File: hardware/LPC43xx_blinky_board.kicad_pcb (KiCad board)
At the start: 4 copper layers, 68 x 49.4 mm, 60 parts, among them J1 Conn_01x04_Male, J2 Conn_ARM_JTAG_SWD_10, J3 USB_B_Micro, J4 Conn_01x20_Female, J5 Micro_SD_Card, J6 Conn_01x04_Female, J7 Conn_01x08_Female, SW1 SW_DIP_x01, SW2 SW_DIP_x04, SW3 SW_SPST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

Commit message: Add final header and silkscreen
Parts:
- added G***: LOGO, Logo:blinky101_logo, B.Cu at (176.8, 93.2)
- added G***: LOGO, Logo:Jitter-med, B.Cu at (169.4, 85.1)
- added J8: Conn_01x16_Female, Connector_PinSocket_2.54mm:PinSocket_1x16_P2.54mm_Vertical, F.Cu at (184.0, 71.9)
- added MH1: MountingHole_Pad, MountingHole:MountingHole_3.2mm_M3_Pad_Via, F.Cu at (115.1, 108.1)
- added MH2: MountingHole_Pad, MountingHole:MountingHole_3.2mm_M3_Pad_Via, F.Cu at (183.6, 66.4)
- J7: footprint Connector_PinSocket_2.54mm:PinSocket_1x08_P2.54mm_Vertical -> Connector_PinSocket_2.54mm:PinSocket_1x09_P2.54mm_Vertical
- moved D1 3.34 mm to (176.5, 68.5)
- moved D2 3.34 mm to (171.8, 68.5)
- moved D3 3.34 mm to (167.8, 68.5)
- moved D4 3.34 mm to (162.0, 68.5)
- moved RN3 3.34 mm to (168.0, 73.8)
- moved J7 1.10 mm to (161.0, 109.6)
- moved SW1 0.25 mm to (120.8, 105.6)
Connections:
- J7 pad 5: Net-(J7-Pad5) -> /AD0
- J7 pad 6: Net-(J7-Pad6) -> /AD1
- J7 pad 7: /AD0 -> /SSP1_SCK
- J7 pad 8: /AD1 -> /SSP1_MISO
- U1 pad 32: Net-(U1-Pad32) -> /SSP1_MISO
- U1 pad 34: Net-(U1-Pad34) -> /SSP1_MOSI
- U1 pad 68: Net-(U1-Pad68) -> /SSP1_SCK
- U1 pad 73: Net-(U1-Pad73) -> /P6_0
- U1 pad 74: Net-(U1-Pad74) -> /P6_1
- U1 pad 78: Net-(U1-Pad78) -> /P6_2
- U1 pad 79: Net-(U1-Pad79) -> /P6_3
- U1 pad 80: Net-(U1-Pad80) -> /P6_4
- U1 pad 82: Net-(U1-Pad82) -> /P6_5
- U1 pad 83: Net-(U1-Pad83) -> /P6_6
- U1 pad 84: Net-(U1-Pad84) -> /P2_2
- U1 pad 85: Net-(U1-Pad85) -> /P6_7
- U1 pad 86: Net-(U1-Pad86) -> /P6_8
- U1 pad 87: Net-(U1-Pad87) -> /P2_3
- U1 pad 88: Net-(U1-Pad88) -> /P2_4
- U1 pad 91: Net-(U1-Pad91) -> /P2_5
- U1 pad 95: Net-(U1-Pad95) -> /P2_6
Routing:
- net /P2_6: track 0.00 -> 41.1 mm, vias 0 -> 1
- net /P2_5: track 0.00 -> 29.2 mm
- net /P2_4: track 0.00 -> 28.7 mm
- net /P6_0: track 0.00 -> 28.5 mm, vias 0 -> 1
- net /P2_3: track 0.00 -> 27.9 mm
- net /P6_1: track 0.00 -> 27.5 mm, vias 0 -> 1
- net /P6_2: track 0.00 -> 27.4 mm
- net /P6_8: track 0.00 -> 27.1 mm
- net /P6_3: track 0.00 -> 26.4 mm
- net /P6_7: track 0.00 -> 26.2 mm
- net /P6_4: track 0.00 -> 25.6 mm
- net /P2_2: track 0.00 -> 25.4 mm
- net /P6_5: track 0.00 -> 24.9 mm
- net /P6_6: track 0.00 -> 24.5 mm
- net /SSP1_SCK: track 0.00 -> 18.7 mm, vias 0 -> 2
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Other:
- board size 68 x 49.4 mm -> 76.2 x 49.5 mm
- board text added: "I2C0"
- board text added: "MISO"
- board text added: "MOSI"
- board text added: "Made in Delft"
- board text added: "P0_0"
- board text added: "P0_1"
- board text added: "P1_19"
- board text added: "P2_0"
- board text added: "P2_1"
- board text added: "P2_2"
- board text added: "P2_3"
- board text added: "P2_4"
- board text added: "P2_5"
- board text added: "P2_6"
- board text added: "P3_1"
- board text added: "P3_2"
- board text added: "P4_7"
- board text added: "P6_0"
- board text added: "P6_1"
- board text added: "P6_2"
- board text added: "P6_3"
- board text added: "P6_4"
- board text added: "P6_5"
- board text added: "P6_6"
- board text added: "P6_7"
- board text added: "P6_8"
- board text added: "P7_4"
- board text added: "P7_5"
- board text added: "P7_6"
- board text added: "P7_7"
- board text added: "PF_4"
- board text added: "RTC_ALARM"
- board text added: "SCK"
- board text added: "SSP1"
- board text added: "SWCLK"
- board text added: "SWDIO"
- board text added: "USART0"
- board text added: "V1.0 lpc43xx"
- board text added: "WakeUP0"
- board text added: "blinky101.github.io"

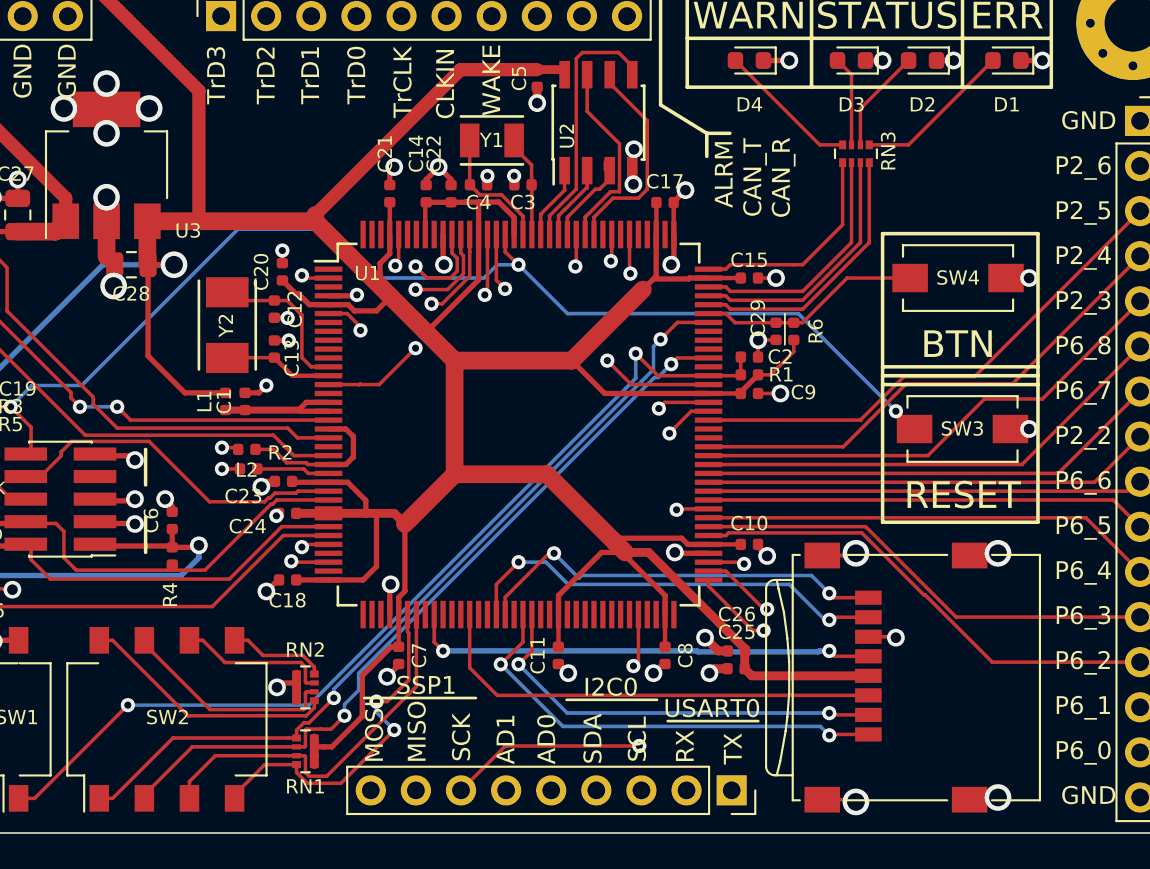
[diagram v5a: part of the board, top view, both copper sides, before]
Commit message: Add missing step files and fix some milimeter work
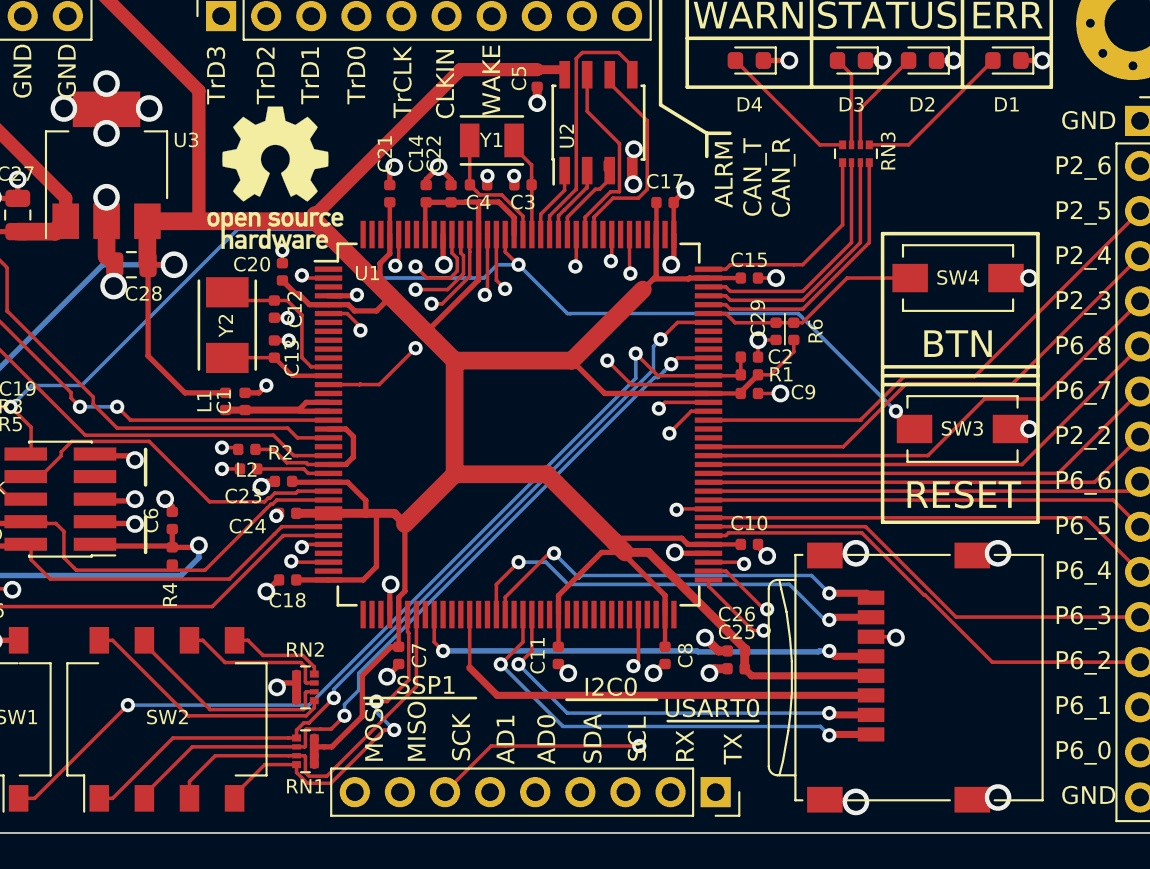
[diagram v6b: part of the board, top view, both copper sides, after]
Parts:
- added REF**: OSHW-Logo_7.5x8mm_SilkScreen, Symbol:OSHW-Logo_7.5x8mm_SilkScreen, F.Cu at (135.3, 75.1)
- moved J7 0.91 mm to (160.1, 109.7)
- moved J5 0.15 mm to (170.4, 103.2)
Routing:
- net /SSP1_SCK: track 18.7 -> 19.7 mm
- net /AD1: track 37.6 -> 36.7 mm
- net /SSP1_MISO: track 18.4 -> 17.6 mm

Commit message: Some silkscreen fixes
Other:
- board text added: "JTAG"
- board text added: "SWD"
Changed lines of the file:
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@@
   (general
     (thickness 1.6)
-    (drawings 118)
+    (drawings 126)
     (tracks 941)
     (zones 0)
@@
     (tags capacitor)
     (attr smd)
-    (fp_text reference C1 (at 0 -1.17 90) (layer F.SilkS)
+    (fp_text reference C1 (at -0.1 1.2 90) (layer F.SilkS)
       (effects (font (size 0.8 0.8) (thickness 0.1)))
     )
@@
     (tags capacitor)
     (attr smd)
-    (fp_text reference C8 (at 0 -1.17 270) (layer F.SilkS)
+    (fp_text reference C8 (at 0 0.85 270) (layer F.SilkS)
       (effects (font (size 0.8 0.8) (thickness 0.1)))
     )
@@
     (tags capacitor)
     (attr smd)
-    (fp_text reference C14 (at 2.25 -0.55 90) (layer F.SilkS)
+    (fp_text reference C14 (at 2.25 -0.8 90) (layer F.SilkS)
       (effects (font (size 0.8 0.8) (thickness 0.1)))
     )
@@
     (tags capacitor)
     (attr smd)
-    (fp_text reference C21 (at 2.25 -0.25 90) (layer F.SilkS)
+    (fp_text reference C21 (at 0 -1 90) (layer F.SilkS)
       (effects (font (size 0.8 0.8) (thickness 0.1)))
     )
@@
     (tags capacitor)
     (attr smd)
-    (fp_text reference C25 (at -0.05 2.05 180) (layer F.SilkS)
+    (fp_text reference C25 (at 2.25 0.15 180) (layer F.SilkS)
       (effects (font (size 0.8 0.8) (thickness 0.1)))
     )
@@
     (tags capacitor)
     (attr smd)
-    (fp_text reference C26 (at -0.035 2.05 180) (layer F.SilkS)
+    (fp_text reference C26 (at 0.065 1.15 180) (layer F.SilkS)
       (effects (font (size 0.8 0.8) (thickness 0.1)))
     )
@@
     (tags resistor)
     (attr smd)
-    (fp_text reference L1 (at 0 -1.17 90) (layer F.SilkS)
+    (fp_text reference L1 (at -0.1 -1.1 90) (layer F.SilkS)
       (effects (font (size 0.8 0.8) (thickness 0.1)))
     )
@@
     (tags resistor)
     (attr smd)
-    (fp_text reference L2 (at 0 -1.17 180) (layer F.SilkS)
+    (fp_text reference L2 (at 2.5 0.2 180) (layer F.SilkS)
       (effects (font (size 0.8 0.8) (thickness 0.1)))
     )
@@
     (tags resistor)
     (attr smd)
-    (fp_text reference R2 (at -1.8 0.9 180) (layer F.SilkS)
+    (fp_text reference R2 (at 2.6 -0.1 180) (layer F.SilkS)
       (effects (font (size 0.8 0.8) (thickness 0.1)))
     )
@@
     (tags "resistor array")
     (attr smd)
-    (fp_text reference RN3 (at -0.146761 -1.845001 270) (layer F.SilkS)
+    (fp_text reference RN3 (at 2 0) (layer F.SilkS)
       (effects (font (size 0.8 0.8) (thickness 0.1)))
     )
@@
       (xy -2.620173 1.933271) (xy -2.53664 1.952468)) (layer F.SilkS) (width 0.01))
   )
-  (gr_text "Made in Delft" (at 153.9 98.3) (layer B.SilkS)
+  (gr_line (start 143.75 75) (end 143.5 74.75) (layer F.SilkS) (width 0.1))
+  (gr_line (start 145.25 74.75) (end 145 74.25) (layer F.SilkS) (width 0.1))
+  (gr_line (start 123.5 88.25) (end 123.5 89.5) (layer F.SilkS) (width 0.2))
+  (gr_line (start 127.75 87.75) (end 123 87.75) (layer F.SilkS) (width 0.2))
+  (gr_line (start 113.25 101.25) (end 113.25 99.75) (layer F.SilkS) (width 0.2))
+  (gr_text SWD (at 115 102.5) (layer F.SilkS)
+    (effects (font (size 1.5 1.5) (thickness 0.3)))
+  )
+  (gr_text JTAG (at 125.25 86.5) (layer F.SilkS)
+    (effects (font (size 1.5 1.5) (thickness 0.3)))
+  )
+  (gr_line (start 161.25 102.75) (end 140.25 102.75) (layer B.SilkS) (width 0.2))
+  (gr_text "Made in Delft" (at 153.9 98.05) (layer B.SilkS)
     (effects (font (size 1.5 1.5) (thickness 0.3)) (justify mirror))
   )
-  (gr_text blinky101.github.io (at 150.9 101.2) (layer B.SilkS)
+  (gr_text blinky101.github.io (at 150.9 100.95) (layer B.SilkS)
     (effects (font (size 1.5 1.5) (thickness 0.3)) (justify mirror))
   )
@@
     (effects (font (size 1 1) (thickness 0.15)) (justify mirror))
   )
-  (gr_line (start 159.6 72.6) (end 160.9 72.6) (layer F.SilkS) (width 0.2))
+  (gr_line (start 159.6 72.6) (end 164.4 72.6) (layer F.SilkS) (width 0.2))
   (gr_line (start 157 71) (end 159.6 72.6) (layer F.SilkS) (width 0.2))
   (gr_line (start 157 64) (end 157 71) (layer F.SilkS) (width 0.2))
   (gr_line (start 150 64) (end 157 64) (layer F.SilkS) (width 0.2))
-  (gr_line (start 159.6 73.9) (end 159.6 72.6) (layer F.SilkS) (width 0.2))
+  (gr_line (start 159.6 76.2) (end 159.6 72.6) (layer F.SilkS) (width 0.2))
   (gr_text GND (at 181.109524 71.9) (layer F.SilkS)
     (effects (font (size 1 1) (thickness 0.15)))

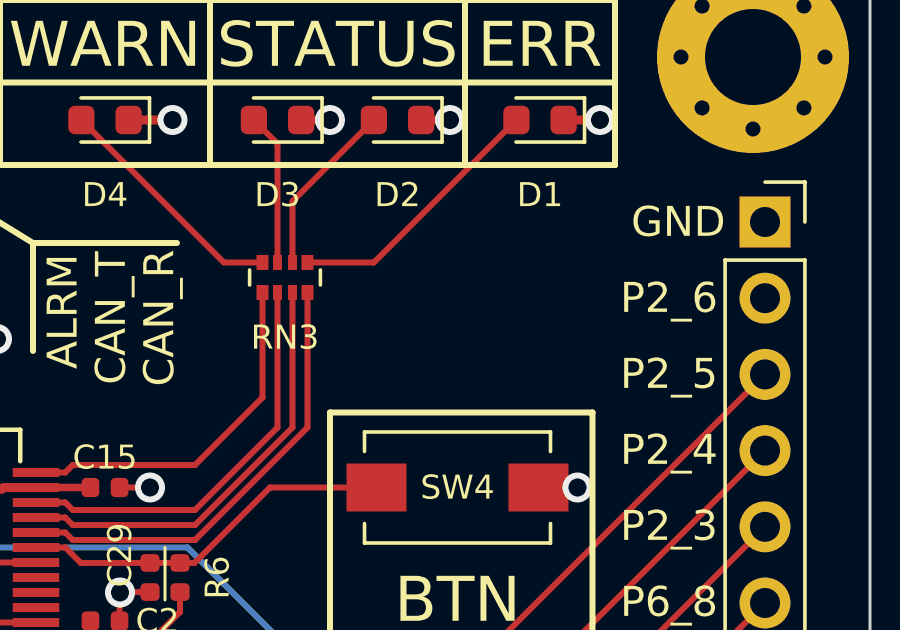
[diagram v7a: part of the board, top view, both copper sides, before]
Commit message: Move 3D shapes to external library. Add renders
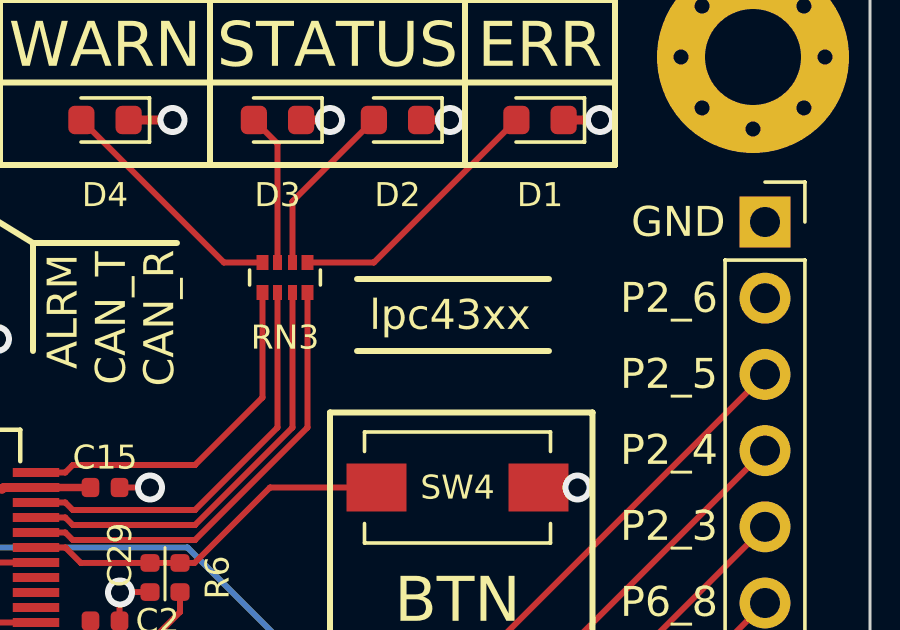
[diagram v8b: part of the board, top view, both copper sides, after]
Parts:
- Y1: footprint misc:Crystal_SMD_Abracon_ABS07-2Pin_3.6x1.9mm -> Jitter_Footprints:Crystal_SMD_Abracon_ABS07-2Pin_3.6x1.9mm
- Y2: footprint Crystal:Crystal_SMD_TXC_7A-2Pin_5.0x3.2mm -> Jitter_Footprints:Crystal_SMD_TXC_7A-2Pin_5.0x3.2mm
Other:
- board text added: "lpc43xx"
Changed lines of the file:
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@@
-(kicad_pcb (version 20171130) (host pcbnew "(5.0.0-3-g5ebb6b6)")
+(kicad_pcb (version 20171130) (host pcbnew "(5.0.1-3-g963ef8bb5)")
   (general
     (thickness 1.6)
-    (drawings 126)
+    (drawings 129)
     (tracks 941)
     (zones 0)
@@
   )
   (setup
-    (last_trace_width 0.4)
+    (last_trace_width 0.2)
     (user_trace_width 0.2)
     (user_trace_width 0.3)
@@
     (pad_drill 0.762)
     (pad_to_mask_clearance 0.075)
+    (solder_mask_min_width 0.25)
     (pad_to_paste_clearance_ratio -0.12)
     (aux_axis_origin 0 0)
@@
     (add_net VBUS)
   )
-  (module misc:Crystal_SMD_Abracon_ABS07-2Pin_3.6x1.9mm (layer F.Cu)
+  (module Jitter_Footprints:Crystal_SMD_Abracon_ABS07-2Pin_3.6x1.9mm (layer F.Cu)
     (at 147.5 73 180)
     (descr https://abracon.com/Resonators/ABS07.pdf)
@@
     (pad 2 smd rect (at 1.25 0 180) (size 1.1 1.9) (layers F.Cu F.Paste F.Mask)
       (net 5 "Net-(C4-Pad2)"))
+    (model :jitter:Crystal_3.2x1.5_ABS07-series.STEP
+      (at (xyz 0 0 0))
+      (scale (xyz 1 1 1))
+      (rotate (xyz -90 0 0))
+    )
+  )
+  (module Jitter_Footprints:Crystal_SMD_TXC_7A-2Pin_5.0x3.2mm (layer F.Cu)
+    (at 132.6 83.4 270)
+    (fp_text reference Y2 (at 0 0.05 270) (layer F.SilkS)
+      (effects (font (size 0.8 0.8) (thickness 0.1)))
+    )
+    (fp_text value 12MHz (at 1.4 3.2 270) (layer F.Fab)
+      (effects (font (size 1 1) (thickness 0.15)))
+    )
+    (fp_line (start 3.2 2.1) (end 3.2 -2.1) (layer F.CrtYd) (width 0.05))
+    (fp_line (start -3.2 2.1) (end 3.2 2.1) (layer F.CrtYd) (width 0.05))
+    (fp_line (start -3.2 -2.1) (end -3.2 2.1) (layer F.CrtYd) (width 0.05))
+    (fp_line (start 3.2 -2.1) (end -3.2 -2.1) (layer F.CrtYd) (width 0.05))
+    (fp_line (start -2.5 1.6) (end 2.5 1.6) (layer F.SilkS) (width 0.15))
+    (fp_line (start -2.5 -1.6) (end 2.5 -1.6) (layer F.SilkS) (width 0.15))
+    (pad 2 smd rect (at 1.85 0 270) (size 1.7 2.4) (layers F.Cu F.Paste F.Mask)
+      (net 8 "Net-(C13-Pad1)"))
+    (pad 1 smd rect (at -1.85 0 270) (size 1.7 2.4) (layers F.Cu F.Paste F.Mask)
+      (net 7 "Net-(C12-Pad1)"))
+    (model :jitter:CRYSTAL_SMD_TXC_7A-2Pin_5.0x3.2mm.step
+      (offset (xyz -2.5 -1.58 0))
+      (scale (xyz 1 1 1))
+      (rotate (xyz 0 0 0))
+    )
   )
   (module Capacitor_SMD:C_0402_1005Metric (layer F.Cu)
@@
     (pad 8 smd rect (at 4.45 -3.81 90) (size 1.5 1.1) (layers F.Cu F.Paste F.Mask)
       (net 49 "Net-(RN2-Pad5)"))
-    (model ${KISYS3DMOD}/Button_Switch_SMD.3dshapes/SW_DIP_SPSTx04_Slide_Omron_A6S-410x_W8.9mm_P2.54mm.wrl
-      (at (xyz 0 0 0))
-      (scale (xyz 1 1 1))
-      (rotate (xyz 0 0 0))
-    )
-    (model ${KIPRJMOD}/A6S-4102-H.step
+    (model :jitter:A6S-4102-H.step
       (at (xyz 0 0 0))
       (scale (xyz 1 1 1))
@@
     )
   )
-  (module Crystal:Crystal_SMD_TXC_7A-2Pin_5.0x3.2mm (layer F.Cu)
-    (at 132.6 83.4 270)
-    (fp_text reference Y2 (at 0 0.05 270) (layer F.SilkS)
-      (effects (font (size 0.8 0.8) (thickness 0.1)))
-    )
-    (fp_text value 12MHz (at 1.4 3.2 270) (layer F.Fab)
-      (effects (font (size 1 1) (thickness 0.15)))
-    )
-    (fp_line (start -2.5 -1.6) (end 2.5 -1.6) (layer F.SilkS) (width 0.15))
-    (fp_line (start -2.5 1.6) (end 2.5 1.6) (layer F.SilkS) (width 0.15))
-    (fp_line (start 3.2 -2.1) (end -3.2 -2.1) (layer F.CrtYd) (width 0.05))
-    (fp_line (start -3.2 -2.1) (end -3.2 2.1) (layer F.CrtYd) (width 0.05))
-    (fp_line (start -3.2 2.1) (end 3.2 2.1) (layer F.CrtYd) (width 0.05))
-    (fp_line (start 3.2 2.1) (end 3.2 -2.1) (layer F.CrtYd) (width 0.05))
-    (pad 1 smd rect (at -1.85 0 270) (size 1.7 2.4) (layers F.Cu F.Paste F.Mask)
-      (net 7 "Net-(C12-Pad1)"))
-    (pad 2 smd rect (at 1.85 0 270) (size 1.7 2.4) (layers F.Cu F.Paste F.Mask)
-      (net 8 "Net-(C13-Pad1)"))
-  )
   (module Button_Switch_SMD:SW_DIP_SPSTx01_Slide_Omron_A6S-110x_W8.9mm_P2.54mm (layer F.Cu)
     (at 120.85 105.6 90)
@@
     (pad 2 smd rect (at 4.45 0 90) (size 1.5 1.1) (layers F.Cu F.Paste F.Mask)
       (net 2 GND))
-    (model ${KISYS3DMOD}/Button_Switch_SMD.3dshapes/SW_DIP_SPSTx01_Slide_Omron_A6S-110x_W8.9mm_P2.54mm.wrl
-      (at (xyz 0 0 0))
-      (scale (xyz 1 1 1))
-      (rotate (xyz 0 0 0))
-    )
-    (model ${KIPRJMOD}/A6S-1102-H.step
+    (model :jitter:A6S-1102-H.step
       (at (xyz 0 0 0))
       (scale (xyz 1 1 1))
@@
     (pad 1 smd rect (at -3.2 -1.55 90) (size 0.8 1.5) (layers F.Cu F.Paste F.Mask)
       (net 23 /SD_DAT2))
-    (model ${KISYS3DMOD}/Connector_Card.3dshapes/microSD_HC_Wuerth_693072010801.wrl
-      (offset (xyz 0 -1.149999983968733 0))
-      (scale (xyz 1 1 1))
-      (rotate (xyz 0 0 0))
-    )
-    (model "${KIPRJMOD}/Micro SD Holder Wurth Elektronik 693072010801.STEP"
+    (model ":jitter:Micro SD Holder Wurth Elektronik 693072010801.step"
       (at (xyz 0 0 0))
       (scale (xyz 1 1 1))
@@
       (xy -2.620173 1.933271) (xy -2.53664 1.952468)) (layer F.SilkS) (width 0.01))
   )
+  (gr_line (start 176.8 73.8) (end 170.4 73.8) (layer F.SilkS) (width 0.2))
+  (gr_line (start 170.4 76.2) (end 176.8 76.2) (layer F.SilkS) (width 0.2))
+  (gr_text lpc43xx (at 173.5 75) (layer F.SilkS)
+    (effects (font (size 1 1) (thickness 0.1)))
+  )
   (gr_line (start 143.75 75) (end 143.5 74.75) (layer F.SilkS) (width 0.1))
